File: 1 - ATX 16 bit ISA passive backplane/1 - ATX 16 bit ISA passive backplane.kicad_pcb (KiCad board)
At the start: 2 copper layers, 161.3 x 181.6 mm, 89 parts, among them J1 BUS 1, J10 AB15, J11 AB15, J12 AB15, J13 AB15, J14 AB15, J15 AB15, J16 AB15, J17 PWR LED, J18 3V BYPASS, J19 ATX POWER, J2 BUS 2, J20 PWR SW, J25 ~{MR} BYPASS, J26 ACT LED, J27 RST SW, J28 RST POL, J29 RST LED, J3 BUS 3, J4 BUS 4, J5 BUS 5, J6 BUS 6, J7 BUS 7, J8 BREADBOARD HEADER (RC2014 COM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, J9 EXTENDED HEADER, SW1 POWER, SW2 RESET, U1 74HCT14, U2 74HCT74, U3 LM7905, U4 74AC174, U6 74AC174

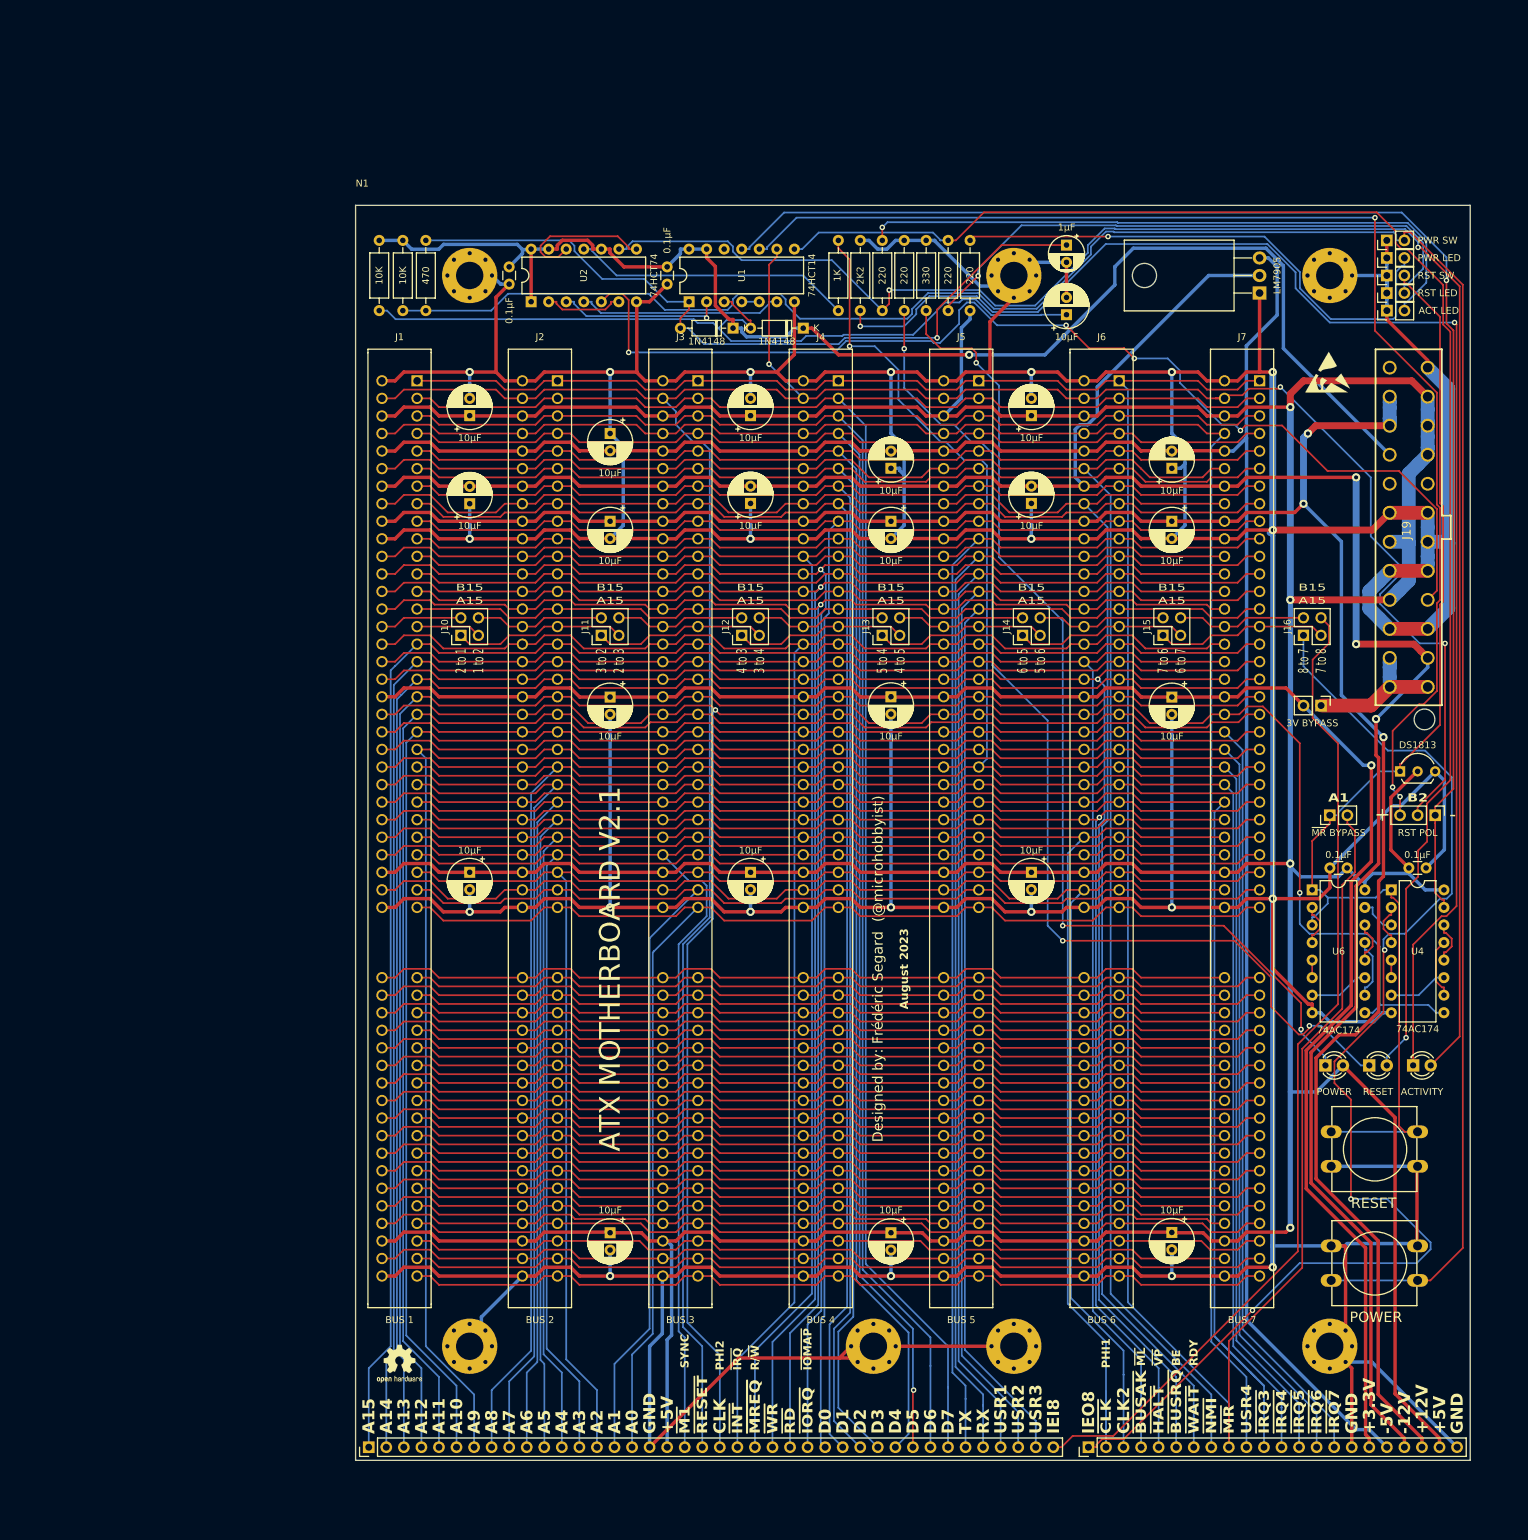
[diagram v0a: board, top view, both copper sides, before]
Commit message: Cleaned up the PCB and ploted the gerber and schematic
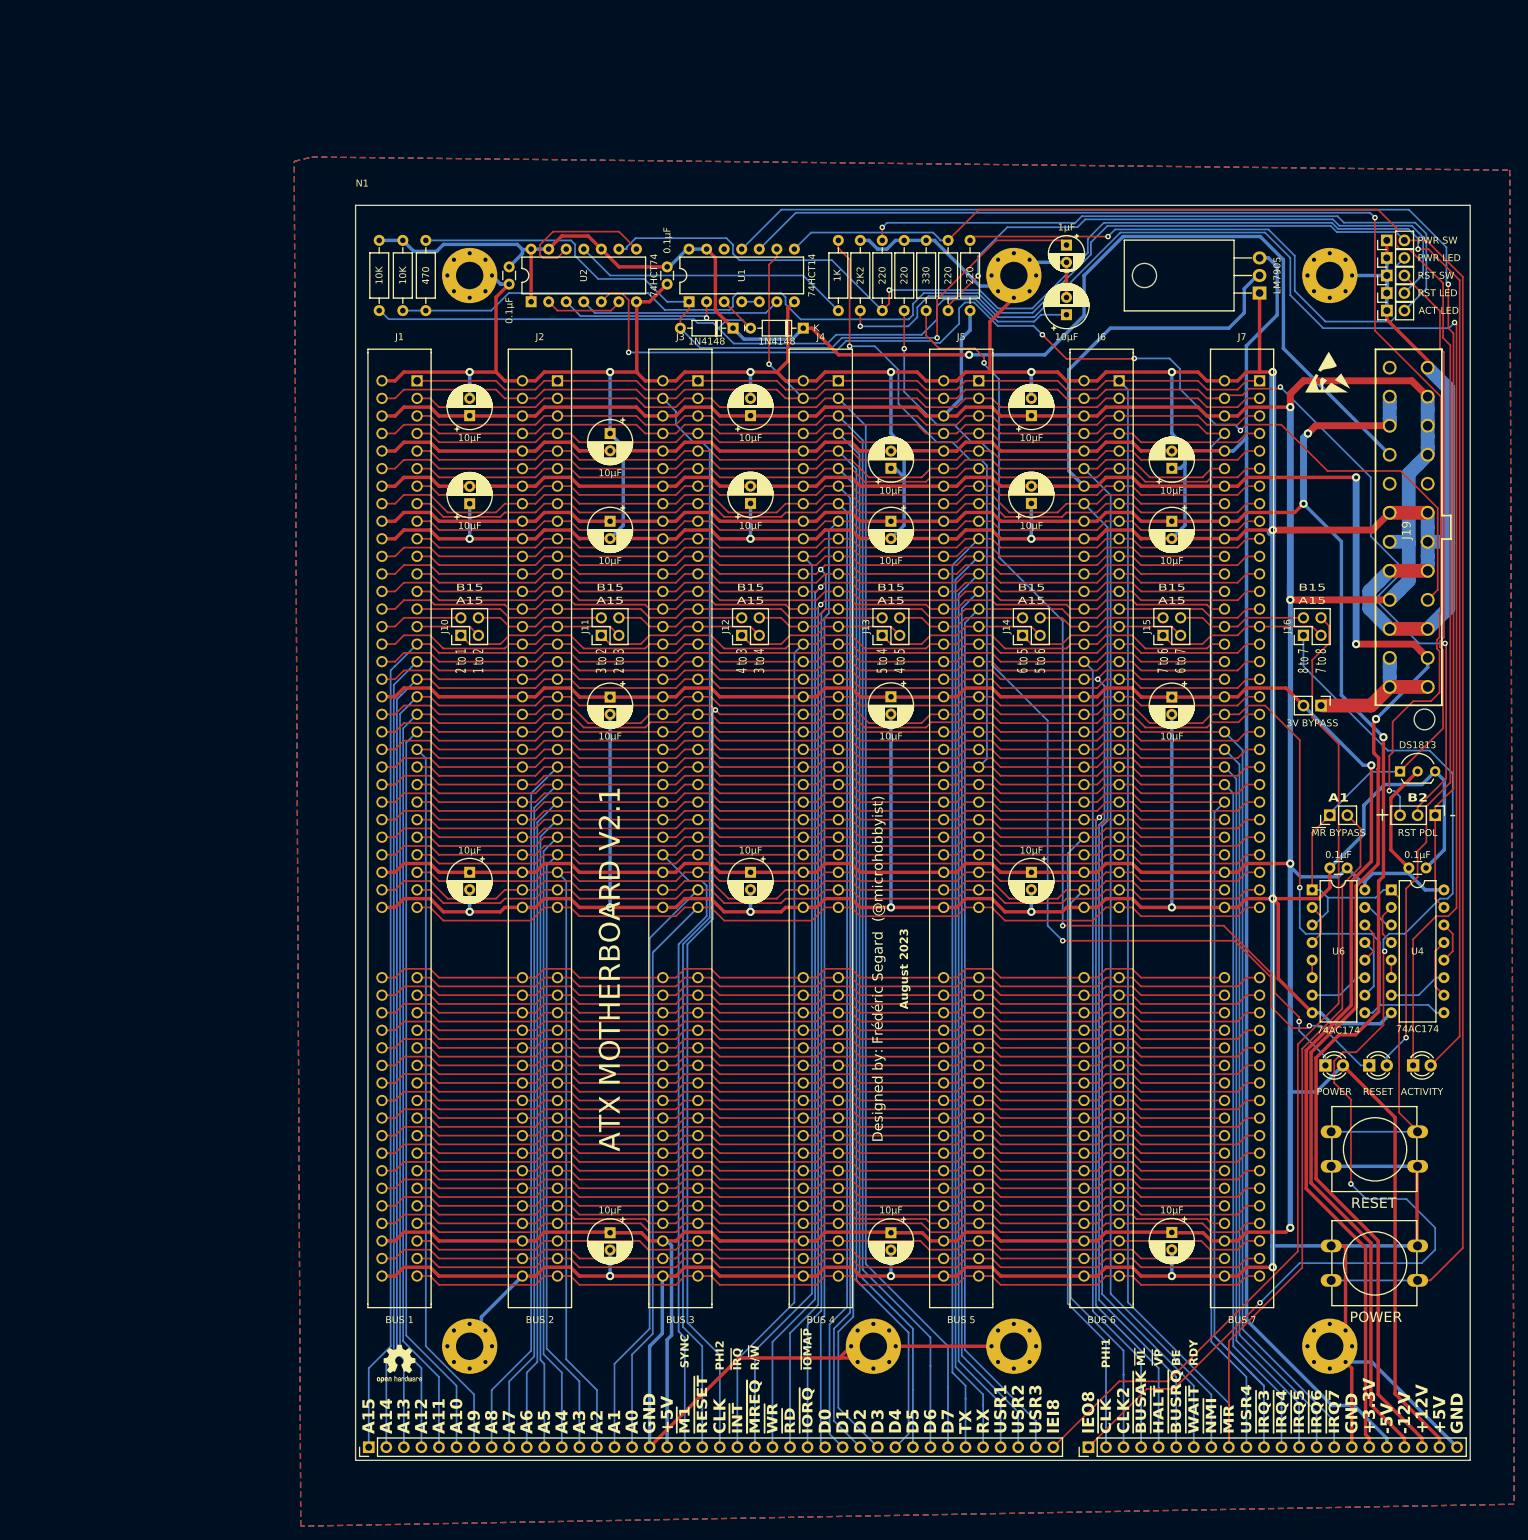
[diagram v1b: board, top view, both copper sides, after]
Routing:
- net -12V: track 358.7 -> 365.0 mm
- net Net-(D4-K): track 212.2 -> 217.7 mm
- net Net-(D4-A): track 253.9 -> 257.1 mm
- net VCC: track 202.6 -> 205.5 mm
- net /IEO8: track 180.4 -> 183.2 mm
- net /Reset & LEDs/+RES: track 185.2 -> 187.9 mm, vias 3 -> 2
- net Net-(J17-Pin_2): track 77.5 -> 80.1 mm
- net Net-(D1-A): track 111.7 -> 114.1 mm
- net Net-(J29-Pin_2): track 84.5 -> 86.5 mm
- net GND: track 1543.5 -> 1545.1 mm
- net /Power/~{PS_ON}: track 161.4 -> 162.7 mm
- net Net-(D2-A): track 116.6 -> 117.9 mm
- net Net-(J20-Pin_2): track 332.5 -> 333.9 mm
- net Net-(J26-Pin_2): track 93.6 -> 94.8 mm
- net Net-(J25-Pin_1): track 169.6 -> 168.5 mm
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- added copper zone on B.Cu, net GND
- added copper zone on F.Cu, net GND

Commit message: Removed unessential components and added capacitors on the bus lanes. Still need work for on the silkscreen side.
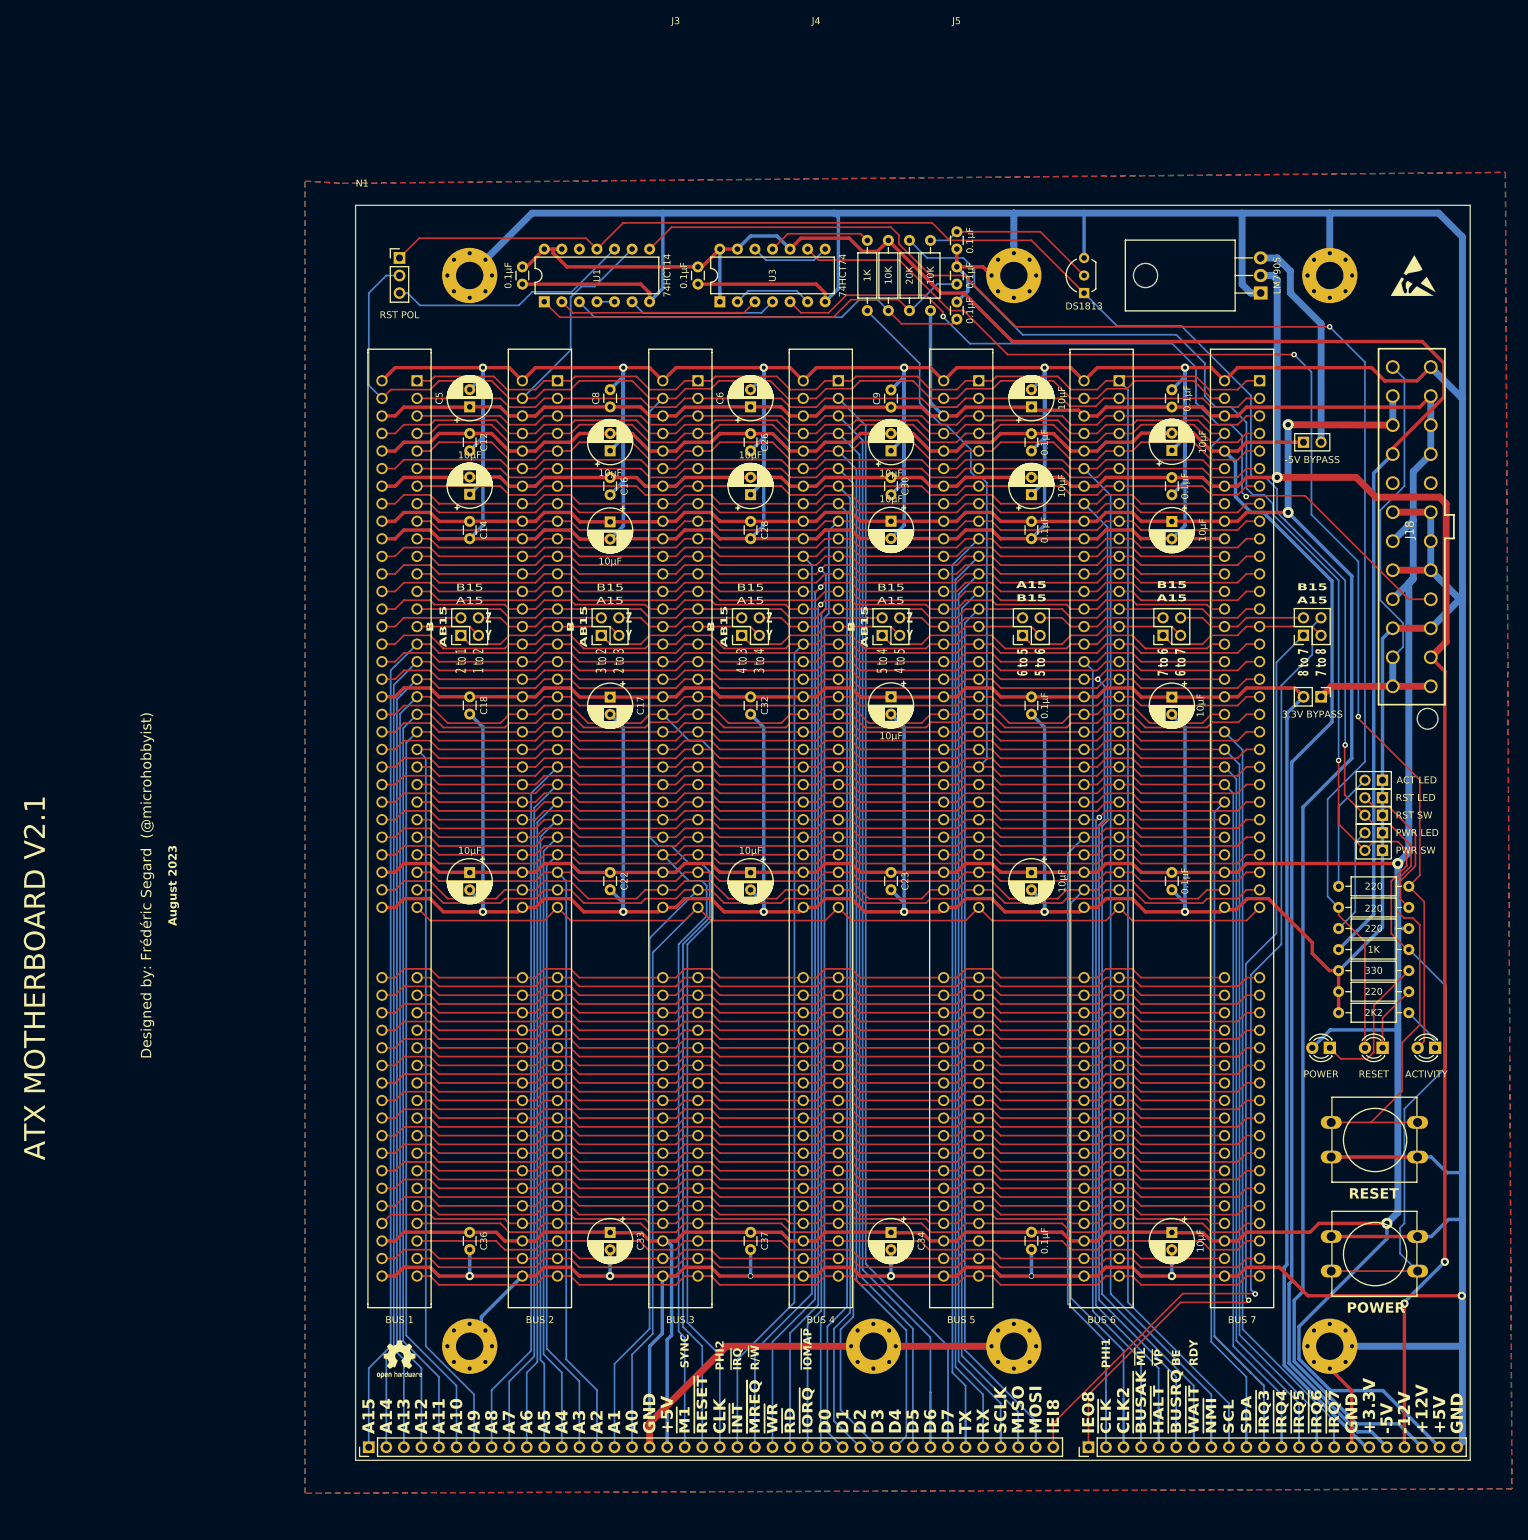
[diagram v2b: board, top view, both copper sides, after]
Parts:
- removed D4: ACTIVITY, LED_THT:LED_D3.0mm
- removed D5: RESET, LED_THT:LED_D3.0mm
- removed J26: ACT LED, Connector_PinHeader_2.54mm:PinHeader_1x02_P2.54mm_Vertical
- removed J27: RST SW, Connector_PinHeader_2.54mm:PinHeader_1x02_P2.54mm_Vertical
- removed J28: RST POL, Connector_PinHeader_2.54mm:PinHeader_1x03_P2.54mm_Vertical
- removed J29: RST LED, Connector_PinHeader_2.54mm:PinHeader_1x02_P2.54mm_Vertical
- removed LOGO7: Logo_Open_Hardware_Small, Symbol:OSHW-Logo2_7.3x6mm_SilkScreen
- removed R12: 220, Resistor_THT:R_Axial_DIN0207_L6.3mm_D2.5mm_P10.16mm_Horizontal
- removed U4, U6: 74AC174, Package_DIP:DIP-16_W7.62mm
- added C16: 0.1µF, Capacitor_THT:C_Disc_D3.0mm_W1.6mm_P2.50mm, F.Cu at (56.5, 54.6)
- added C17: 10µF, Capacitor_THT:CP_Radial_D6.3mm_P2.50mm, F.Cu at (56.5, 86.4)
- added C32: 0.1µF, Capacitor_THT:C_Disc_D3.0mm_W1.6mm_P2.50mm, F.Cu at (76.8, 86.4)
- added C33: 10µF, Capacitor_THT:CP_Radial_D6.3mm_P2.50mm, F.Cu at (56.5, 163.9)
- added C34: 10µF, Capacitor_THT:CP_Radial_D6.3mm_P2.50mm, F.Cu at (97.2, 163.9)
- added C35: 10µF, Capacitor_THT:CP_Radial_D6.3mm_P2.50mm, F.Cu at (137.8, 163.9)
- added C36: 0.1µF, Capacitor_THT:C_Disc_D3.0mm_W1.6mm_P2.50mm, F.Cu at (36.2, 163.8)
- added C37: 0.1µF, Capacitor_THT:C_Disc_D3.0mm_W1.6mm_P2.50mm, F.Cu at (76.8, 163.8)
- added C38: 0.1µF, Capacitor_THT:C_Disc_D3.0mm_W1.6mm_P2.50mm, F.Cu at (117.5, 163.8)
- added C39: 10µF, Capacitor_THT:CP_Radial_D6.3mm_P2.50mm, F.Cu at (137.8, 50.7)
- added C40: 0.1µF, Capacitor_THT:C_Disc_D3.0mm_W1.6mm_P2.50mm, F.Cu at (117.5, 48.3)
- added C41: 10µF, Capacitor_THT:CP_Radial_D6.3mm_P2.50mm, F.Cu at (137.8, 61.0)
- added C42: 0.1µF, Capacitor_THT:C_Disc_D3.0mm_W1.6mm_P2.50mm, F.Cu at (117.5, 61.0)
- added C43: 10µF, Capacitor_THT:CP_Radial_D6.3mm_P2.50mm, F.Cu at (117.5, 57.1)
- added C44: 0.1µF, Capacitor_THT:C_Disc_D3.0mm_W1.6mm_P2.50mm, F.Cu at (137.8, 54.6)
- added C45: 10µF, Capacitor_THT:CP_Radial_D6.3mm_P2.50mm, F.Cu at (137.8, 86.4)
- added C46: 0.1µF, Capacitor_THT:C_Disc_D3.0mm_W1.6mm_P2.50mm, F.Cu at (117.5, 86.4)
- added C47: 0.1µF, Capacitor_THT:C_Disc_D3.0mm_W1.6mm_P2.50mm, F.Cu at (106.7, 19.1)
- added C7: 10µF, Capacitor_THT:CP_Radial_D6.3mm_P2.50mm, F.Cu at (117.5, 44.4)
- added C8: 0.1µF, Capacitor_THT:C_Disc_D3.0mm_W1.6mm_P2.50mm, F.Cu at (56.5, 44.4)
- added J21: RST POL, Connector_PinHeader_2.54mm:PinHeader_1x03_P2.54mm_Vertical, F.Cu at (26.0, 22.9)
- added J22: ACT LED, 0 - Library:PinHeader_1x2_Vertical (Modified), F.Cu at (168.3, 98.4)
- added J23: RST SW, 0 - Library:PinHeader_1x2_Vertical (Modified), F.Cu at (168.3, 103.5)
- added J24: RST LED, 0 - Library:PinHeader_1x2_Vertical (Modified), F.Cu at (168.3, 101.0)
- added LOGO6: Logo_Open_Hardware_Small, Symbol:ESD-Logo_6.6x6mm_SilkScreen, B.Cu at (173.0, 25.4)
- added R6: 220, Resistor_THT:R_Axial_DIN0207_L6.3mm_D2.5mm_P10.16mm_Horizontal, F.Cu at (172.1, 113.8)
- added R7: 2K2, Resistor_THT:R_Axial_DIN0207_L6.3mm_D2.5mm_P10.16mm_Horizontal, F.Cu at (172.1, 132.1)
- C1: value 1µF -> 0.1µF; footprint Capacitor_THT:CP_Radial_D5.0mm_P2.50mm -> Capacitor_THT:C_Disc_D3.0mm_W1.6mm_P2.50mm
- C10, C12, C14, C18, C2, C22, C23, C24, C26, C28, C30, C9: value 10µF -> 0.1µF; footprint Capacitor_THT:CP_Radial_D6.3mm_P2.50mm -> Capacitor_THT:C_Disc_D3.0mm_W1.6mm_P2.50mm
- C5, C6: value 0.1µF -> 10µF; footprint Capacitor_THT:C_Disc_D3.0mm_W1.6mm_P2.50mm -> Capacitor_THT:CP_Radial_D6.3mm_P2.50mm
- D1: value 1N4148 -> ACTIVITY; footprint Diode_THT:D_DO-35_SOD27_P7.62mm_Horizontal -> LED_THT:LED_D3.0mm
- D2: value 1N4148 -> RESET; footprint Diode_THT:D_DO-35_SOD27_P7.62mm_Horizontal -> LED_THT:LED_D3.0mm
- J10, J11, J12, J13: footprint 0 - Library:PinHeader_2x02_Vertical -> 0 - Library:PinHeader_2x2_Vertical (Modified)
- J14: value AB15 -> B15; footprint 0 - Library:PinHeader_2x02_Vertical -> 0 - Library:PinHeader_2x2_Vertical (Modified)
- J15, J16: value AB15 -> A15; footprint 0 - Library:PinHeader_2x02_Vertical -> 0 - Library:PinHeader_2x2_Vertical (Modified)
- J17: value PWR LED -> 3.3V BYPASS
- J18: value 3V BYPASS -> ATX POWER; footprint Connector_PinHeader_2.54mm:PinHeader_1x02_P2.54mm_Vertical -> 0 - Library:ATX_PSU_CONN
- J19: value ATX POWER -> -5V BYPASS; footprint 0 - Library:ATX_PSU_CONN -> 0 - Library:PinHeader_1x2_Vertical (Modified)
- J20: footprint Connector_PinHeader_2.54mm:PinHeader_1x02_P2.54mm_Vertical -> 0 - Library:PinHeader_1x2_Vertical (Modified)
- J25: value ~{MR} BYPASS -> PWR LED; footprint Connector_PinHeader_2.54mm:PinHeader_1x02_P2.54mm_Vertical -> 0 - Library:PinHeader_1x2_Vertical (Modified)
- LOGO1: footprint Symbol:OSHW-Logo2_7.3x6mm_SilkScreen -> 0 - Library:MicroHobbyist; moved to B.Cu
- LOGO2: footprint 0 - Library:MicroHobbyist -> Symbol:OSHW-Logo2_7.3x6mm_SilkScreen; moved to F.Cu
- LOGO5: footprint Symbol:ESD-Logo_6.6x6mm_SilkScreen -> Symbol:OSHW-Logo2_7.3x6mm_SilkScreen
- R11: value 220 -> 330
- R2: value 10K -> 1K
- R3: value 470 -> 20K
- R4: value 330 -> 1K
- R5: value 220 -> 10K
- R8: value 1K -> 220
- R9: value 2K2 -> 220
- U2: value 74HCT74 -> LM7905; footprint Package_DIP:DIP-14_W7.62mm -> Package_TO_SOT_THT:TO-220-3_Horizontal_TabDown
- U3: value LM7905 -> 74HCT74; footprint Package_TO_SOT_THT:TO-220-3_Horizontal_TabDown -> Package_DIP:DIP-14_W7.62mm
- moved LOGO5 196.3 mm to (26.0, 182.2)
- moved R2 172.6 mm to (161.9, 122.9), turned to 0 degrees
- moved D1 145.5 mm to (175.9, 137.2)
- moved C5 143.4 mm to (36.2, 44.4), turned to 90 degrees
- moved D2 133.7 mm to (168.3, 137.2)
- moved R9 126.5 mm to (172.1, 129.0), turned to 180 degrees
- moved C25 120.2 mm to (97.2, 50.8), turned to 90 degrees
- moved R11 120.2 mm to (172.1, 126.0), turned to 180 degrees
- moved R8 119.5 mm to (172.1, 116.8), turned to 180 degrees
- moved C26 117.4 mm to (76.8, 48.3)
- moved C6 116.3 mm to (76.8, 44.4), turned to 90 degrees
- moved R10 111.1 mm to (161.9, 119.9), turned to 0 degrees
- moved C27 110.6 mm to (97.2, 61.0)
- moved U2 105.6 mm to (150.6, 27.9)
- moved J20 88.3 mm to (168.3, 108.6), turned to -90 degrees
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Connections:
- C1 pad 1: Net-(D1-A) -> VCC
- C11 pad 1: +5V -> GND
- C11 pad 2: GND -> -5V
- C12 pad 1: GND -> -5V
- C12 pad 2: -5V -> GND
- C14 pad 1: GND -> +12V
- C14 pad 2: -12V -> GND
- C15 pad 1: +3V3 -> GND
- C15 pad 2: GND -> -12V
- C18 pad 1: +5V -> +3V3
- C2 pad 1: Net-(D2-A) -> VCC
- C21 pad 1: GND -> +5V
- C21 pad 2: -5V -> GND
- C22 pad 1: +12V -> +5V
- C23 pad 1: GND -> +5V
- C23 pad 2: -12V -> GND
- C24 pad 1: +3V3 -> +5V
- C25 pad 1: +5V -> GND
- C25 pad 2: GND -> -5V
- C26 pad 1: +5V -> -5V
- C27 pad 1: +5V -> +12V
- C28 pad 1: GND -> +12V
- C28 pad 2: -5V -> GND
- C29 pad 1: +12V -> GND
- C29 pad 2: GND -> -12V
- C3 pad 1: VCC -> Net-(C3-Pad1)
- C30 pad 1: GND -> -12V
- C30 pad 2: -12V -> GND
- C4 pad 1: VCC -> Net-(C4-Pad1)
- D1 pad 1: VCC -> Net-(D1-K)
- D2 pad 1: VCC -> Net-(D2-K)
- J1 pad 1: /~{MR} -> /SCL
- J1 pad 12: /USR1 -> /SCLK
- J1 pad 13: /USR2 -> /MISO
- J1 pad 14: /USR3 -> /MOSI
- J1 pad 35: /USR4 -> /SDA
- J1 pad 63: /USR5 -> /TX2
- J1 pad 72: /USR6 -> /RX2
- J1 pad 81: /USR7 -> /USR1
- J1 pad 82: /USR8 -> /USR2
- J1 pad 87: /~{IRQ14} -> /~{IRQ15}
- J1 pad 88: /~{IRQ15} -> /~{IRQ14}
- J1 pad 89: /MOSI -> /USR3
- J1 pad 90: /MISO -> /USR4
- J1 pad 91: /SCLK -> /USR5
- J1 pad 92: /~{SS} -> /USR6
- J1 pad 93: /SCL -> /USR7
- J1 pad 94: /SDA -> /USR8
- J17 pad 1: GND -> /Power/3V3
- J17 pad 2: Net-(J17-Pin_2) -> +3V3
- J18 pad 2: +3V3 -> /Power/3V3
- J19 pad 1: /Power/3V3 -> -5V
- J19 pad 2: /Power/3V3 -> Net-(J19-Pin_2)
- J2 pad 1: /~{MR} -> /SCL
- J2 pad 12: /USR1 -> /SCLK
- J2 pad 13: /USR2 -> /MISO
- J2 pad 14: /USR3 -> /MOSI
- J2 pad 35: /USR4 -> /SDA
- J2 pad 63: /USR5 -> /TX2
- J2 pad 72: /USR6 -> /RX2
- J2 pad 81: /USR7 -> /USR1
- J2 pad 82: /USR8 -> /USR2
- J2 pad 87: /~{IRQ14} -> /~{IRQ15}
- J2 pad 88: /~{IRQ15} -> /~{IRQ14}
- J2 pad 89: /MOSI -> /USR3
- J2 pad 90: /MISO -> /USR4
- J2 pad 91: /SCLK -> /USR5
- J2 pad 92: /~{SS} -> /USR6
- J2 pad 93: /SCL -> /USR7
- J2 pad 94: /SDA -> /USR8
- J25 pad 1: Net-(J25-Pin_1) -> GND
- J25 pad 2: /~{MR} -> Net-(J25-Pin_2)
- J3 pad 1: /~{MR} -> /SCL
- J3 pad 12: /USR1 -> /SCLK
- J3 pad 13: /USR2 -> /MISO
- J3 pad 14: /USR3 -> /MOSI
- J3 pad 35: /USR4 -> /SDA
- J3 pad 63: /USR5 -> /TX2
- J3 pad 72: /USR6 -> /RX2
- J3 pad 81: /USR7 -> /USR1
- J3 pad 82: /USR8 -> /USR2
- J3 pad 87: /~{IRQ14} -> /~{IRQ15}
- J3 pad 88: /~{IRQ15} -> /~{IRQ14}
- J3 pad 89: /MOSI -> /USR3
- J3 pad 90: /MISO -> /USR4
- J3 pad 91: /SCLK -> /USR5
- J3 pad 92: /~{SS} -> /USR6
- J3 pad 93: /SCL -> /USR7
- J3 pad 94: /SDA -> /USR8
- J4 pad 1: /~{MR} -> /SCL
- J4 pad 12: /USR1 -> /SCLK
- J4 pad 13: /USR2 -> /MISO
- J4 pad 14: /USR3 -> /MOSI
- J4 pad 35: /USR4 -> /SDA
- J4 pad 63: /USR5 -> /TX2
- J4 pad 72: /USR6 -> /RX2
- J4 pad 81: /USR7 -> /USR1
- J4 pad 82: /USR8 -> /USR2
- J4 pad 87: /~{IRQ14} -> /~{IRQ15}
- J4 pad 88: /~{IRQ15} -> /~{IRQ14}
- J4 pad 89: /MOSI -> /USR3
- J4 pad 90: /MISO -> /USR4
- J4 pad 91: /SCLK -> /USR5
- J4 pad 92: /~{SS} -> /USR6
- J4 pad 93: /SCL -> /USR7
- J4 pad 94: /SDA -> /USR8
- J5 pad 1: /~{MR} -> /SCL
- J5 pad 12: /USR1 -> /SCLK
- J5 pad 13: /USR2 -> /MISO
- J5 pad 14: /USR3 -> /MOSI
- J5 pad 35: /USR4 -> /SDA
- J5 pad 63: /USR5 -> /TX2
- J5 pad 72: /USR6 -> /RX2
- J5 pad 81: /USR7 -> /USR1
- J5 pad 82: /USR8 -> /USR2
- J5 pad 87: /~{IRQ14} -> /~{IRQ15}
- J5 pad 88: /~{IRQ15} -> /~{IRQ14}
- J5 pad 89: /MOSI -> /USR3
- J5 pad 90: /MISO -> /USR4
- J5 pad 91: /SCLK -> /USR5
- J5 pad 92: /~{SS} -> /USR6
- J5 pad 93: /SCL -> /USR7
- J5 pad 94: /SDA -> /USR8
- J6 pad 1: /~{MR} -> /SCL
- J6 pad 12: /USR1 -> /SCLK
- J6 pad 13: /USR2 -> /MISO
- J6 pad 14: /USR3 -> /MOSI
- J6 pad 35: /USR4 -> /SDA
- J6 pad 63: /USR5 -> /TX2
- J6 pad 72: /USR6 -> /RX2
- J6 pad 81: /USR7 -> /USR1
- J6 pad 82: /USR8 -> /USR2
- J6 pad 87: /~{IRQ14} -> /~{IRQ15}
- J6 pad 88: /~{IRQ15} -> /~{IRQ14}
- J6 pad 89: /MOSI -> /USR3
- J6 pad 90: /MISO -> /USR4
- J6 pad 91: /SCLK -> /USR5
- J6 pad 92: /~{SS} -> /USR6
- J6 pad 93: /SCL -> /USR7
- J6 pad 94: /SDA -> /USR8
- J7 pad 1: /~{MR} -> /SCL
- J7 pad 12: /USR1 -> /SCLK
- J7 pad 13: /USR2 -> /MISO
- J7 pad 14: /USR3 -> /MOSI
- J7 pad 35: /USR4 -> /SDA
- J7 pad 63: /USR5 -> /TX2
- J7 pad 72: /USR6 -> /RX2
- J7 pad 81: /USR7 -> /USR1
- J7 pad 82: /USR8 -> /USR2
- J7 pad 87: /~{IRQ14} -> /~{IRQ15}
- J7 pad 88: /~{IRQ15} -> /~{IRQ14}
- J7 pad 89: /MOSI -> /USR3
- J7 pad 90: /MISO -> /USR4
- J7 pad 91: /SCLK -> /USR5
- J7 pad 92: /~{SS} -> /USR6
- J7 pad 93: /SCL -> /USR7
- J7 pad 94: /SDA -> /USR8
- J8 pad 37: /USR1 -> /SCLK
- J8 pad 38: /USR2 -> /MISO
- J8 pad 39: /USR3 -> /MOSI
- J9 pad 10: /USR4 -> /SDA
- J9 pad 9: /~{MR} -> /SCL
- R1 pad 2: Net-(J20-Pin_2) -> Net-(C3-Pad1)
- R10 pad 1: Net-(D4-A) -> Net-(J25-Pin_2)
- R10 pad 2: Net-(J26-Pin_2) -> +5V
- R11 pad 1: Net-(D5-K) -> Net-(D3-K)
- R2 pad 2: Net-(D2-A) -> Net-(J20-Pin_2)
- R3 pad 1: Net-(D1-A) -> Net-(J20-Pin_2)
- R3 pad 2: Net-(J20-Pin_2) -> Net-(C4-Pad1)
- R4 pad 1: Net-(D3-K) -> Net-(U3B-C)
- R4 pad 2: GND -> /A8
- R5 pad 1: Net-(J17-Pin_2) -> +5V
- R5 pad 2: +5V -> Net-(RS1-VCC)
- R8 pad 1: Net-(U2B-C) -> Net-(J24-Pin_2)
- R8 pad 2: /A8 -> Net-(D2-A)
- R9 pad 1: Net-(D4-K) -> Net-(D2-K)
- RS1 pad 1: Net-(J25-Pin_1) -> /Reset & LEDs/-RST
- RS1 pad 2: +5V -> Net-(RS1-VCC)
- SW2 pad 1: Net-(J25-Pin_1) -> /Reset & LEDs/-RST
- U1 pad 1: Net-(D1-A) -> Net-(C4-Pad1)
- U1 pad 10: /Reset & LEDs/+RES -> /Reset & LEDs/+RST
- U1 pad 11: /Reset & LEDs/-RES -> /Reset & LEDs/-RST
- U1 pad 2: Net-(U2A-C) -> Net-(U3A-C)
- U1 pad 3: Net-(D2-A) -> Net-(C3-Pad1)
- U1 pad 6: Net-(U2A-~{S}) -> /Power/~{PWR_UP}
- U1 pad 8: Net-(D5-A) -> Net-(D2-A)
- U2 pad 1: VCC -> GND
- U2 pad 2: Net-(U2A-D) -> -12V
- U2 pad 3: Net-(U2A-C) -> Net-(J19-Pin_2)
- U3 pad 1: GND -> VCC
- U3 pad 2: -12V -> Net-(U3A-D)
- U3 pad 3: -5V -> Net-(U3A-C)
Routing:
- net GND: track 1545.1 -> 2077.0 mm, vias 22 -> 19
- net /~{MR}: track 389.2 -> 0.00 mm
- net /Reset & LEDs/-RST: track 0.00 -> 272.7 mm, vias 0 -> 1
- net Net-(D4-A): track 257.1 -> 0.00 mm, vias 2 -> 0
- net Net-(D5-A): track 220.6 -> 0.00 mm, vias 1 -> 0
- net Net-(D4-K): track 217.7 -> 0.00 mm, vias 2 -> 0
- net /Reset & LEDs/-RES: track 204.2 -> 0.00 mm, vias 1 -> 0
- net /Reset & LEDs/+RES: track 187.9 -> 0.00 mm, vias 2 -> 0
- net Net-(J25-Pin_1): track 168.5 -> 0.00 mm
- net /SCL: track 128.2 -> 295.5 mm
- net /SDA: track 128.2 -> 286.1 mm
- net Net-(D5-K): track 157.5 -> 0.00 mm, vias 3 -> 0
- net /USR4: track 277.8 -> 128.2 mm
- net /SCLK: track 128.2 -> 261.5 mm
- net /MISO: track 128.2 -> 259.0 mm
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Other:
- board text added: "MISO"
- board text added: "MOSI"
- board text added: "SCL"
- board text added: "SCLK"
- board text added: "SDA"
- board text removed: "5 to 6"
- board text removed: "6 to 5"
- board text removed: "6 to 7"
- board text removed: "7 to 6"
- board text removed: "7 to 8"
- board text removed: "8 to 7"
- board text removed: "USR1"
- board text removed: "USR2"
- board text removed: "USR3"
- board text removed: "USR4"
- board text removed: "~{MR}"
